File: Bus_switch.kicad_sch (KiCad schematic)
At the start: 7 parts, among them J3 Conn_01x04_Pin, U1 SN74CB3Q3384APW

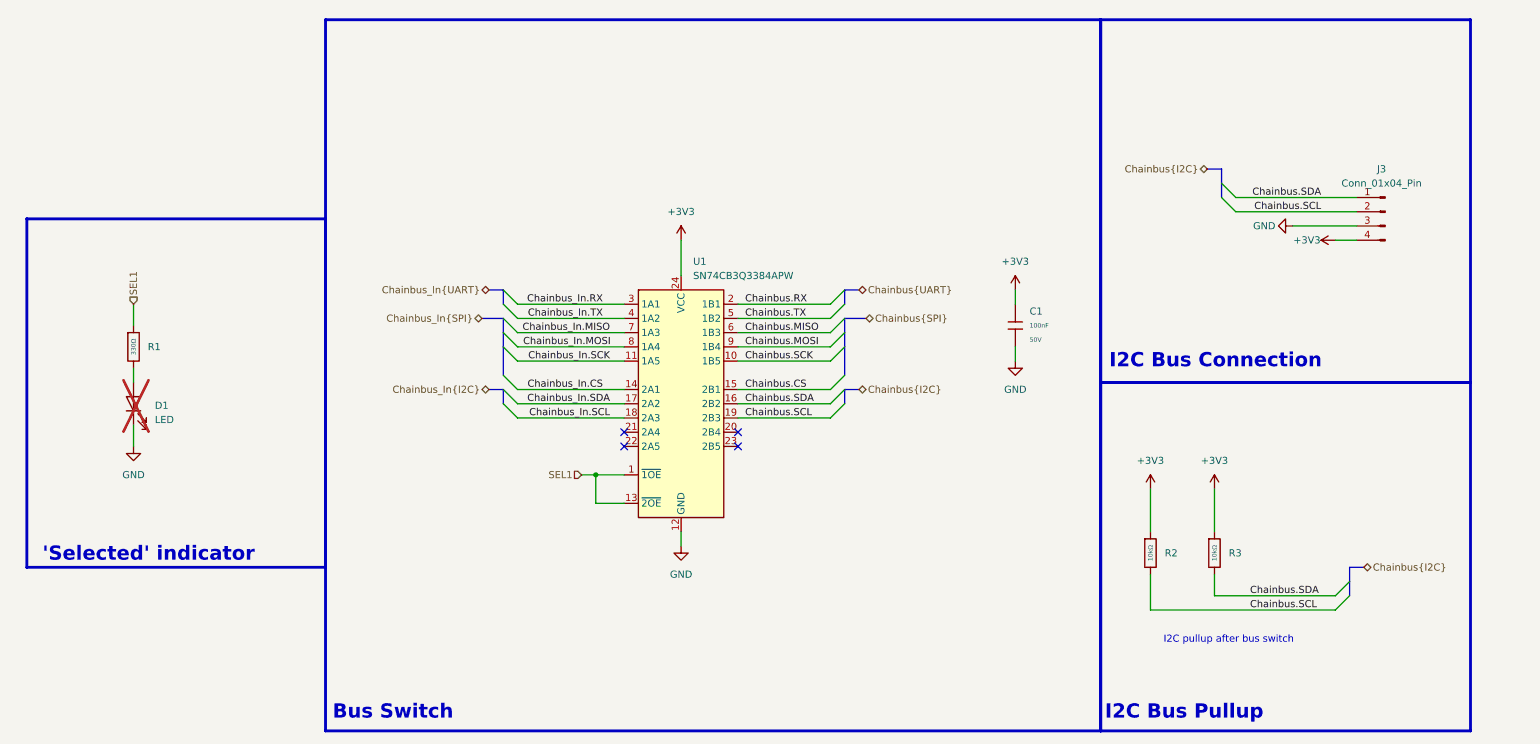
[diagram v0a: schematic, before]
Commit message: fixed selected led polarity
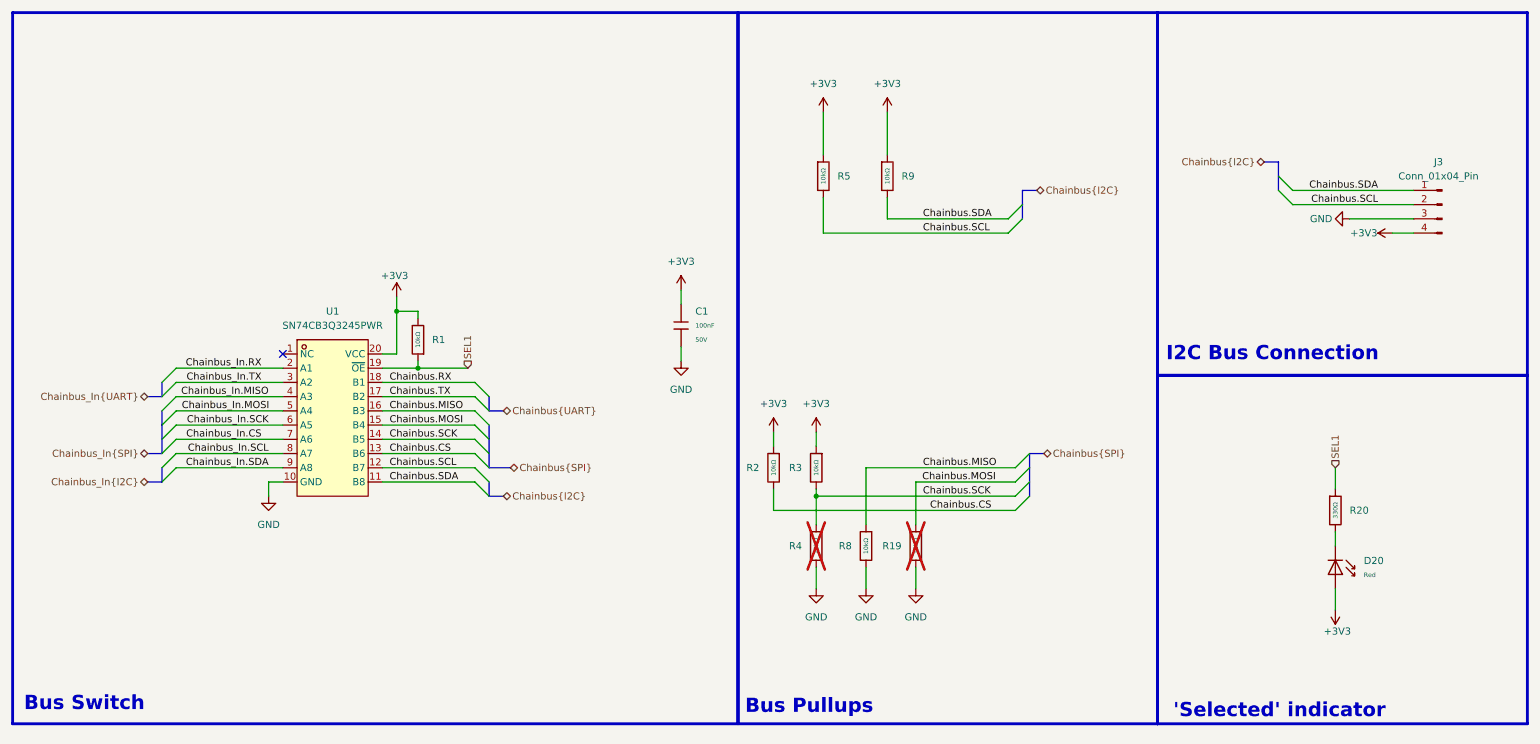
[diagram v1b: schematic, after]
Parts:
- removed D1: LED, LED_SMD:LED_0603_1608Metric, symbol Device:LED
- removed U1: SN74CB3Q3384APW, Package_SO:TSSOP-24_4.4x7.8mm_P0.65mm, symbol 74xx:SN74CB3Q3384APW
- added D20: Red, PCM_JLCPCB:D_0603, symbol PCM_JLCPCB-Diodes:LED,0603,Red
- added R1, R19, R2, R3, R4, R8: 10kΩ, PCM_JLCPCB:R_0402, symbol PCM_JLCPCB-Resistors:0402,10kΩ
- added U1: SN74CB3Q3245PWR, SN74CB3Q3245PWR:TSSOP-20_L6.5-W4.4-P0.65-LS6.4-BL, symbol SN74CB3Q3245PWR:SN74CB3Q3245PWR
- renumbered R1 to R20, R2 to R5, R3 to R9
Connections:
- net +3V3: now also D20.2, R1.2, R2.1, R3.1, U1.20 (VCC)
- net Chainbus.CS: now also R2.2, U1.13 (B6)
- net Chainbus.MISO: now also R8.1, U1.16 (B3)
- net Chainbus.MOSI: now also R19.1, U1.15 (B4)
- net Chainbus.RX: now also U1.18 (B1)
- net Chainbus.SCK: now also R3.2, R4.1, U1.14 (B5)
- net Chainbus.SCL: now also U1.12 (B7)
- net Chainbus.SDA: now also U1.11 (B8)
- net Chainbus.TX: now also U1.17 (B2)
- net Chainbus_In.CS: now also U1.7 (A6)
- net Chainbus_In.MISO: now also U1.4 (A3)
- net Chainbus_In.MOSI: now also U1.5 (A4)
- net Chainbus_In.RX: now also U1.2 (A1)
- net Chainbus_In.SCK: now also U1.6 (A5)
- net Chainbus_In.SCL: now also U1.8 (A7)
- net Chainbus_In.SDA: now also U1.9 (A8)
- net Chainbus_In.TX: now also U1.3 (A2)
- net GND: now also R19.2, R4.2, R8.2, U1.10 (GND)
- net SEL1: now also R1.1, U1.19 (~{OE})
- net at R20.2: now also D20.1
- no-connect marks 4 -> 1
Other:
- note added: "Bus Pullups"
- note removed: "I2C Bus Pullup"
- note removed: "I2C pullup after bus switch"
- title: MMS3 Stepper Controler -> MMS3 Hat template small (Change Me)
- moved on the sheet: C1, J3, R20, R5, R9
